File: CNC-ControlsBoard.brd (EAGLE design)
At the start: 99.1 x 83.8 mm, 42 parts, among them IC1 ATTINY84-20PU, IC2 MAX7219CNG, IC3 74HCT4053P, IC4 74HCT165N, IC5 74HCT165N, IC6 74HCT157N, IC7 74HC148N

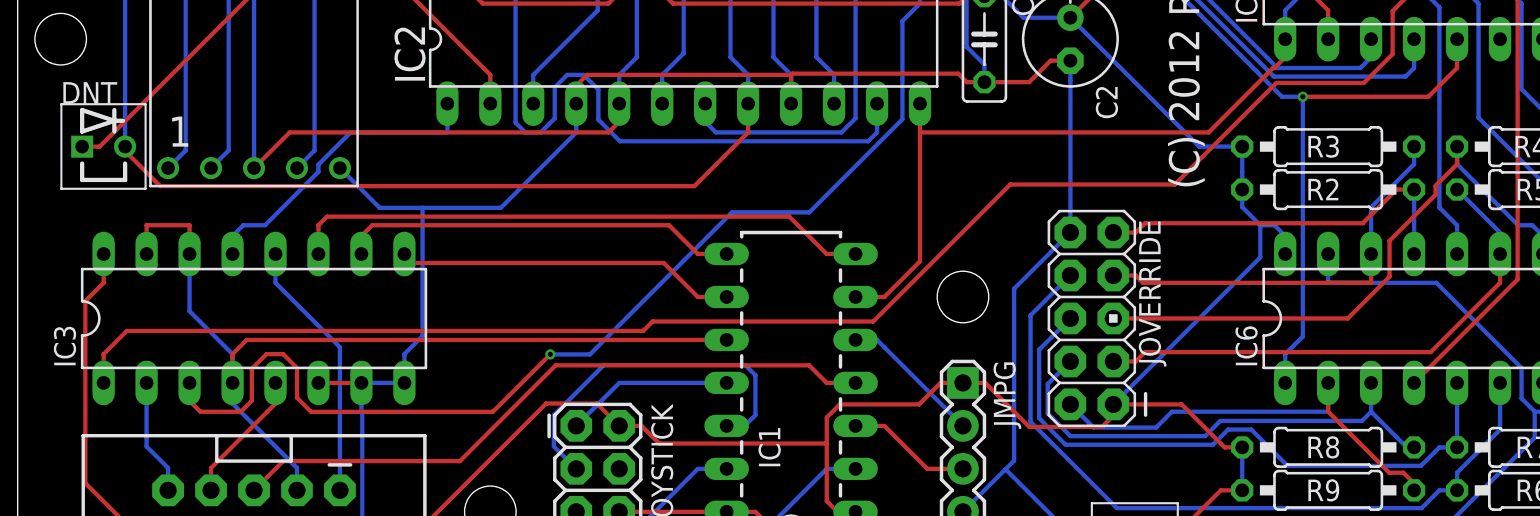
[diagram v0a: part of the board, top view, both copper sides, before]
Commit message: Housekeeping: - deleted obsolete Interface and Main -only boards and schematics. All these have been condensed in the MainStepInterface panel now - updated .gitignore to include library backups - updated symbol of 7-segment display to make it smaller - minor touch-ups on Controls PCB
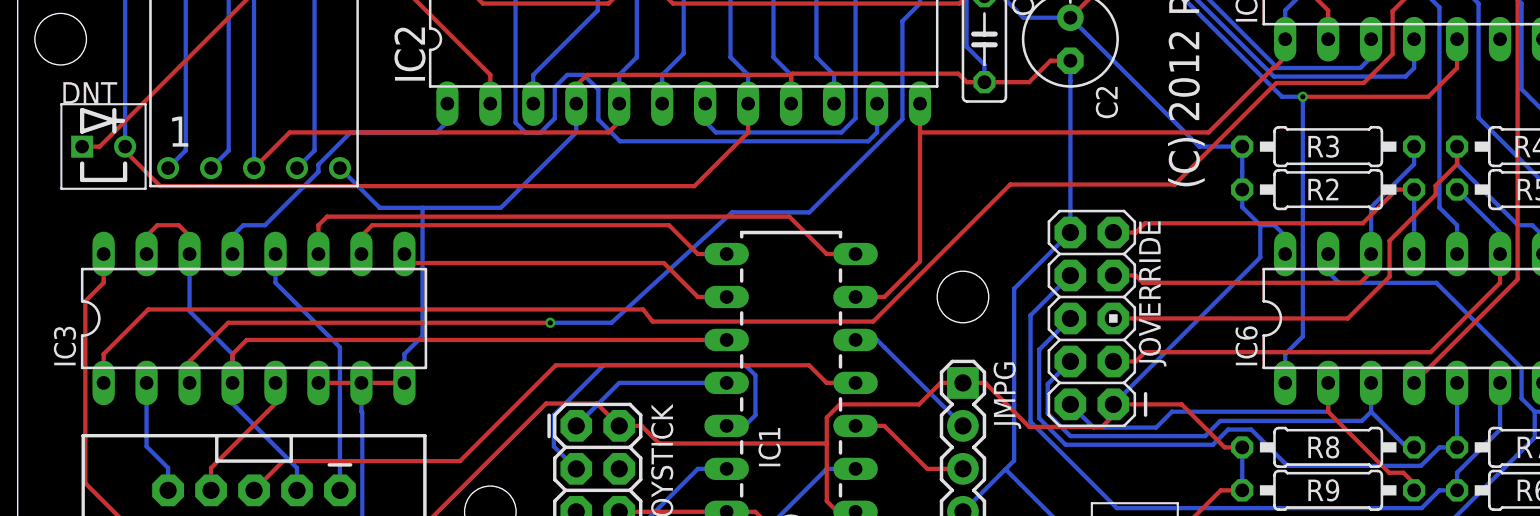
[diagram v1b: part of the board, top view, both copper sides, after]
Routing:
- net SCK_OUT: track 109.2 -> 102.8 mm
- net !SS: track 53.8 -> 53.1 mm
- net SROUT: track 104.8 -> 105.4 mm
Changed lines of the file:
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@@
 <?xml version="1.0" encoding="utf-8"?>
 <!DOCTYPE eagle SYSTEM "eagle.dtd">
-<eagle version="6.3">
+<eagle version="6.4">
 <drawing>
 <settings>
@@
 <setting verticaltext="up"/>
 </settings>
-<grid distance="0.05" unitdist="inch" unit="inch" style="lines" multiple="1" display="no" altdistance="0.005" altunitdist="inch" altunit="inch"/>
+<grid distance="0.05" unitdist="inch" unit="inch" style="lines" multiple="1" display="yes" altdistance="0.005" altunitdist="inch" altunit="inch"/>
 <layers>
 <layer number="1" name="Top" color="4" fill="1" visible="yes" active="yes"/>
@@
 <wire x1="88.9" y1="11.7816" x2="88.9" y2="13.5831" width="0.254" layer="16"/>
 <wire x1="88.9" y1="13.5831" x2="83.865" y2="18.6181" width="0.254" layer="16"/>
-<wire x1="83.865" y1="18.6181" x2="77.47" y2="18.6181" width="0.254" layer="16"/>
+<wire x1="77.47" y1="20.32" x2="77.47" y2="19.2531" width="0.254" layer="16"/>
+<wire x1="77.47" y1="19.2531" x2="78.105" y2="18.6181" width="0.254" layer="16"/>
+<wire x1="78.105" y1="18.6181" x2="83.865" y2="18.6181" width="0.254" layer="16"/>
 <wire x1="92.71" y1="12.7" x2="92.71" y2="11.6331" width="0.254" layer="16"/>
 <wire x1="92.71" y1="11.6331" x2="92.075" y2="10.9981" width="0.254" layer="16"/>
@@
 <wire x1="64.1096" y1="2.54" x2="63.4491" y2="2.54" width="0.254" layer="16"/>
 <wire x1="64.77" y1="2.54" x2="64.1096" y2="2.54" width="0.254" layer="16"/>
-<wire x1="77.47" y1="20.32" x2="77.47" y2="18.6181" width="0.254" layer="16"/>
 <wire x1="78.74" y1="52.5019" x2="78.74" y2="43.6119" width="0.254" layer="1"/>
 <wire x1="78.74" y1="43.6119" x2="77.47" y2="42.3419" width="0.254" layer="1"/>
@@
 <wire x1="20.6086" y1="67.5986" x2="19.05" y2="66.04" width="0.254" layer="1"/>
 <wire x1="35.56" y1="5.08" x2="41.91" y2="5.08" width="0.254" layer="1"/>
-<wire x1="20.32" y1="12.7" x2="22.86" y2="12.7" width="0.254" layer="16"/>
+<wire x1="20.32" y1="12.7" x2="22.86" y2="12.7" width="0.254" layer="1"/>
 <wire x1="17.78" y1="12.7" x2="20.32" y2="12.7" width="0.254" layer="1"/>
 </signal>
@@
 <wire x1="10.16" y1="20.32" x2="10.16" y2="16.9419" width="0.254" layer="16"/>
 <wire x1="10.16" y1="16.9419" x2="12.7" y2="14.4019" width="0.254" layer="16"/>
-<wire x1="10.16" y1="20.32" x2="10.16" y2="22.0219" width="0.254" layer="1"/>
-<wire x1="7.62" y1="20.32" x2="7.62" y2="22.0219" width="0.254" layer="1"/>
-<wire x1="7.62" y1="22.0219" x2="10.16" y2="22.0219" width="0.254" layer="1"/>
+<wire x1="8.255" y1="22.0219" x2="9.525" y2="22.0219" width="0.254" layer="1"/>
+<wire x1="9.525" y1="22.0219" x2="10.16" y2="21.3869" width="0.254" layer="1"/>
+<wire x1="10.16" y1="21.3869" x2="10.16" y2="20.32" width="0.254" layer="1"/>
+<wire x1="7.62" y1="20.32" x2="7.62" y2="21.3869" width="0.254" layer="1"/>
+<wire x1="7.62" y1="21.3869" x2="8.255" y2="22.0219" width="0.254" layer="1"/>
 <wire x1="13.1828" y1="10.9981" x2="12.7" y2="11.4809" width="0.254" layer="16"/>
 <wire x1="12.7" y1="11.4809" x2="12.7" y2="12.7" width="0.254" layer="16"/>
@@
 <wire x1="58.675" y1="24.4289" x2="50.5764" y2="16.3303" width="0.254" layer="1"/>
 <wire x1="50.5764" y1="16.3303" x2="37.5313" y2="16.3303" width="0.254" layer="1"/>
-<wire x1="37.5313" y1="16.3303" x2="36.9743" y2="15.7733" width="0.254" layer="1"/>
-<wire x1="36.9743" y1="15.7733" x2="6.4514" y2="15.7733" width="0.254" layer="1"/>
-<wire x1="6.4514" y1="15.7733" x2="5.08" y2="14.4019" width="0.254" layer="1"/>
+<wire x1="37.5313" y1="16.3303" x2="36.9743" y2="17.0433" width="0.254" layer="1"/>
+<wire x1="36.9743" y1="17.0433" x2="7.7214" y2="17.0433" width="0.254" layer="1"/>
+<wire x1="7.7214" y1="17.0433" x2="5.08" y2="14.4019" width="0.254" layer="1"/>
 </signal>
 <signal name="DCIN">
 <contactref element="IC2" pad="1"/>
 <contactref element="IC3" pad="13"/>
-<wire x1="25.4" y1="29.21" x2="25.4" y2="27.5081" width="0.254" layer="16"/>
+<wire x1="19.679" y1="27.5081" x2="24.765" y2="27.5081" width="0.254" layer="16"/>
+<wire x1="24.765" y1="27.5081" x2="25.4" y2="28.1431" width="0.254" layer="16"/>
+<wire x1="25.4" y1="28.1431" x2="25.4" y2="29.21" width="0.254" layer="16"/>
 <wire x1="12.7" y1="20.32" x2="12.7" y2="21.3869" width="0.254" layer="16"/>
 <wire x1="12.7" y1="21.3869" x2="13.335" y2="22.0219" width="0.254" layer="16"/>
@@
 <wire x1="17.78" y1="25.181" x2="17.78" y2="25.6091" width="0.254" layer="16"/>
 <wire x1="17.78" y1="25.6091" x2="19.679" y2="27.5081" width="0.254" layer="16"/>
-<wire x1="19.679" y1="27.5081" x2="25.4" y2="27.5081" width="0.254" layer="16"/>
 </signal>
 <signal name="SCK_OUT">
@@
 <wire x1="77.47" y1="50.8" x2="77.47" y2="49.0981" width="0.254" layer="1"/>
 <wire x1="53.34" y1="36.83" x2="53.34" y2="35.1281" width="0.254" layer="16"/>
-<wire x1="13.1972" y1="10.9981" x2="10.795" y2="10.9981" width="0.254" layer="1"/>
-<wire x1="10.795" y1="10.9981" x2="10.16" y2="11.6331" width="0.254" layer="1"/>
-<wire x1="10.16" y1="11.6331" x2="10.16" y2="12.7" width="0.254" layer="1"/>
-<wire x1="31.483" y1="14.3864" x2="28.086" y2="10.9894" width="0.254" layer="1"/>
-<wire x1="28.086" y1="10.9894" x2="17.3442" y2="10.9894" width="0.254" layer="1"/>
-<wire x1="17.3442" y1="10.9894" x2="16.51" y2="11.8236" width="0.254" layer="1"/>
-<wire x1="16.51" y1="11.8236" x2="16.51" y2="13.5842" width="0.254" layer="1"/>
-<wire x1="16.51" y1="13.5842" x2="15.6923" y2="14.4019" width="0.254" layer="1"/>
-<wire x1="15.6923" y1="14.4019" x2="14.7067" y2="14.4019" width="0.254" layer="1"/>
-<wire x1="14.7067" y1="14.4019" x2="13.8391" y2="13.5343" width="0.254" layer="1"/>
-<wire x1="13.8391" y1="13.5343" x2="13.8391" y2="11.64" width="0.254" layer="1"/>
-<wire x1="13.8391" y1="11.64" x2="13.1972" y2="10.9981" width="0.254" layer="1"/>
-<via x="31.483" y="14.3864" extent="1-16" drill="0.3048" diameter="0.6096"/>
+<via x="31.483" y="16.256" extent="1-16" drill="0.3048" diameter="0.6096"/>
 <wire x1="53.34" y1="35.1281" x2="52.2985" y2="34.0866" width="0.254" layer="16"/>
 <wire x1="52.2985" y1="34.0866" x2="52.2985" y2="28.2824" width="0.254" layer="16"/>
 <wire x1="52.2985" y1="28.2824" x2="46.7989" y2="22.7828" width="0.254" layer="16"/>
 <wire x1="46.7989" y1="22.7828" x2="42.2273" y2="22.7828" width="0.254" layer="16"/>
-<wire x1="42.2273" y1="22.7828" x2="33.8309" y2="14.3864" width="0.254" layer="16"/>
-<wire x1="33.8309" y1="14.3864" x2="31.483" y2="14.3864" width="0.254" layer="16"/>
+<wire x1="42.2273" y1="22.7828" x2="35.1009" y2="16.256" width="0.254" layer="16"/>
+<wire x1="35.1009" y1="16.256" x2="31.483" y2="16.256" width="0.254" layer="16"/>
+<wire x1="31.483" y1="16.256" x2="12.446" y2="16.256" width="0.254" layer="1"/>
+<wire x1="12.446" y1="16.256" x2="10.16" y2="13.97" width="0.254" layer="1"/>
+<wire x1="10.16" y1="13.97" x2="10.16" y2="12.7" width="0.254" layer="1"/>
 </signal>
 <signal name="SOA1">
@@
 <contactref element="IC6" pad="14"/>
 <wire x1="64.77" y1="19.05" x2="66.0909" y2="19.05" width="0.254" layer="1"/>
-<wire x1="80.01" y1="20.32" x2="80.01" y2="18.6181" width="0.254" layer="1"/>
-<wire x1="80.01" y1="18.6181" x2="66.5228" y2="18.6181" width="0.254" layer="1"/>
+<wire x1="80.01" y1="20.32" x2="80.01" y2="19.2531" width="0.254" layer="1"/>
+<wire x1="80.01" y1="19.2531" x2="79.375" y2="18.6181" width="0.254" layer="1"/>
+<wire x1="79.375" y1="18.6181" x2="66.5228" y2="18.6181" width="0.254" layer="1"/>
 <wire x1="66.5228" y1="18.6181" x2="66.0909" y2="19.05" width="0.254" layer="1"/>
 <wire x1="82.55" y1="26.67" x2="82.55" y2="25.6285" width="0.254" layer="16"/>

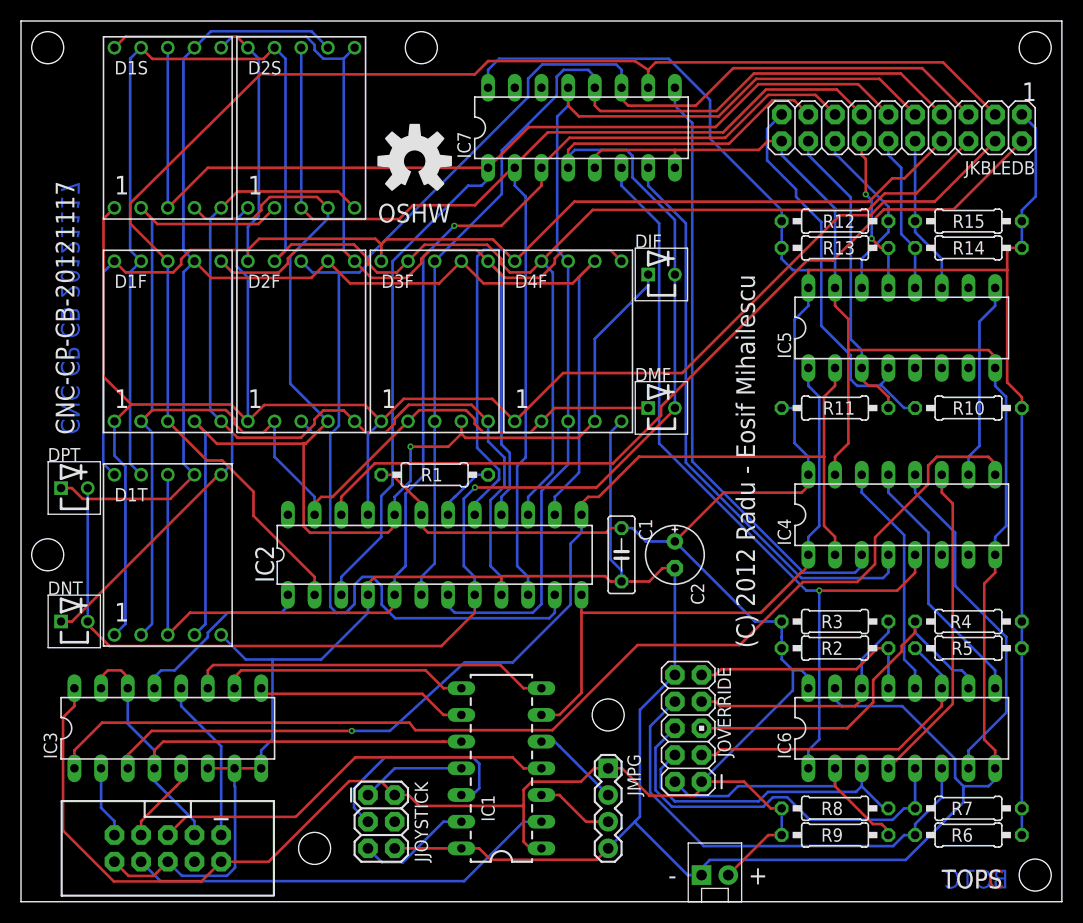
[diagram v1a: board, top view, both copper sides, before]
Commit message: BUGFIX: Same 4053 mistake fixed on Controls board as well UPDATE: 27k instead of 33k for Riset as all LEDs can handle 20mA at 2.1V - routed both DRO and Controls in FreeRouting - updated silkscreen/artwork to reflect new revision - still needs to fix DRU checks (FreeRouting always sees non-PTH holes smaller)
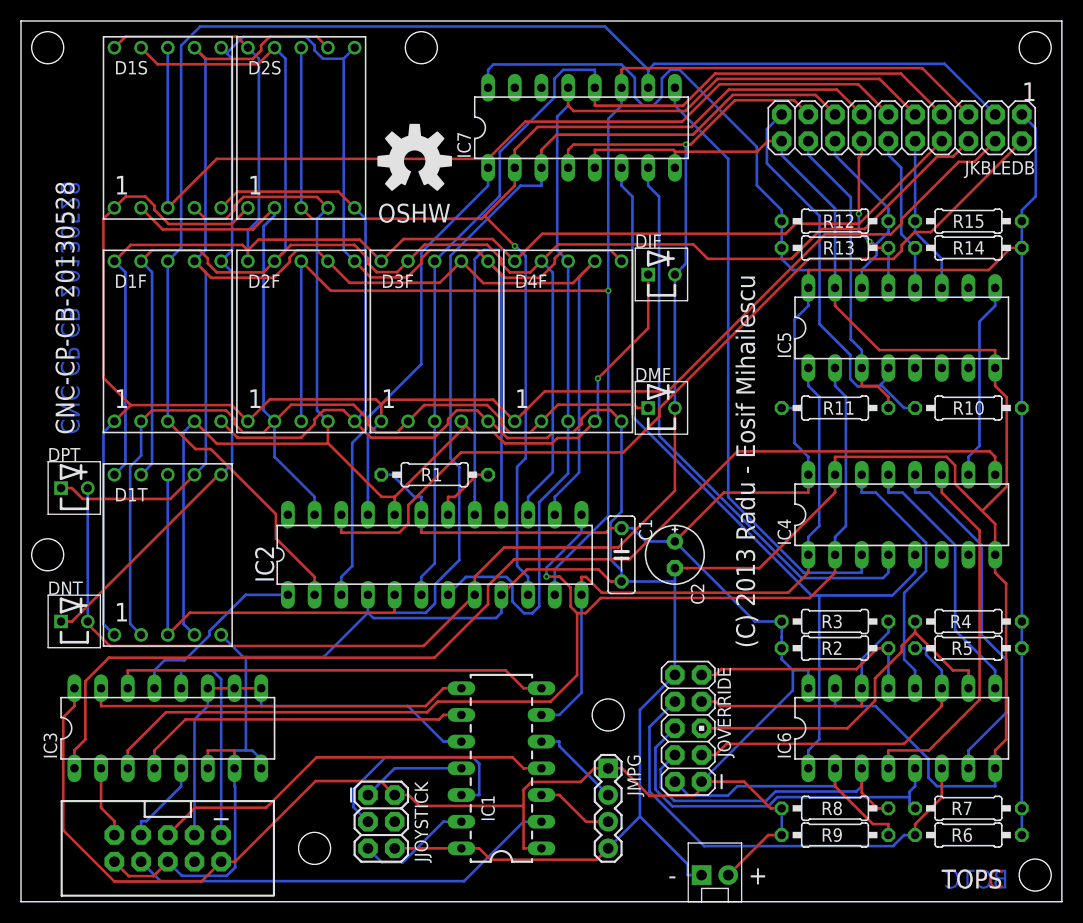
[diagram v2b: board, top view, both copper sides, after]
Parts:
- R1: value 33k -> 27k
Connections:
- net !SS: now also IC3.10, IC3.11, IC3.9; no longer IC3.14, IC3.15, IC3.4
- net MISO_INT: now also IC3.15; no longer IC3.10
- net MOSI_INT: now also IC3.14; no longer IC3.11
- net SCK_INT: now also IC3.4; no longer IC3.9
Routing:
- net MISO_INT: track 23.6 -> 36.7 mm
- net SCK_INT: track 20.1 -> 32.3 mm
- net SEGAC: track 134.9 -> 122.9 mm
- net !SS: track 53.1 -> 41.7 mm
- net DIGA1: track 144.3 -> 133.1 mm, vias 0 -> 1
- net DIGA7: track 147.4 -> 137.2 mm
- net SCK_OUT: track 102.8 -> 112.5 mm
- net MOSI_INT: track 34.6 -> 41.8 mm
- net VCC: track 352.8 -> 359.7 mm
- net DIGA0: track 137.6 -> 143.3 mm
- net DIGA6: track 119.8 -> 125.4 mm, vias 1 -> 0
- net SEGAB: track 147.0 -> 152.4 mm
- net SEGAE: track 171.3 -> 166.1 mm
- net MOSI: track 15.5 -> 20.7 mm
- net SEGAF: track 178.4 -> 173.4 mm
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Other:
- board text added: "(C) 2013 Radu - Eosif Mihailescu"
- board text added: "CNC-CP-CB-20130528"
- board text removed: "(C) 2012 Radu - Eosif Mihailescu"
- board text removed: "CNC-CP-CB-20121117"
